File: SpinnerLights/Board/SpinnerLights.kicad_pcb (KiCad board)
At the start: 2 copper layers, 0 parts

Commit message: SpinnerLights: Initial board generation
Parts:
- added BT1: BAT-HLD-001-THM, BAT_BAT-HLD-001-THM, F.Cu at (197.2, 74.2)
- added BT2: BAT-HLD-001-THM, BAT_BAT-HLD-001-THM, F.Cu at (197.2, 54.9)
- added C1: 0.1uF, Capacitor_SMD:C_0805_2012Metric, F.Cu at (196.6, 85.4)
- added D1: D, Diode_SMD:D_0603_1608Metric_Pad1.05x0.95mm_HandSolder, F.Cu at (239.4, 51.6)
- added JP1: Jumper_2_Open, Jumper:SolderJumper-2_P1.3mm_Open_RoundedPad1.0x1.5mm, F.Cu at (239.3, 54.6)
- added JP2: Jumper_2_Open, Jumper:SolderJumper-2_P1.3mm_Open_RoundedPad1.0x1.5mm, F.Cu at (218.8, 75.8)
- added PIXEL2: NeoPixel_THT, LED_SMD:LED_SK6812MINI_PLCC4_3.5x3.5mm_P1.75mm, F.Cu at (213.1, 76.5)
- added PIXEL3: NeoPixel_THT, LED_SMD:LED_SK6812MINI_PLCC4_3.5x3.5mm_P1.75mm, F.Cu at (240.7, 47.7)
- added PIXEL4: NeoPixel_THT, LED_SMD:LED_SK6812MINI_PLCC4_3.5x3.5mm_P1.75mm, F.Cu at (213.1, 71.5)
- added PIXEL5: NeoPixel_THT, LED_SMD:LED_SK6812MINI_PLCC4_3.5x3.5mm_P1.75mm, F.Cu at (233.6, 52.8)
- added PIXEL6: NeoPixel_THT, LED_SMD:LED_SK6812MINI_PLCC4_3.5x3.5mm_P1.75mm, F.Cu at (220.1, 71.5)
- added Pixel1: NeoPixel_THT, LED_SMD:LED_SK6812MINI_PLCC4_3.5x3.5mm_P1.75mm, F.Cu at (233.6, 47.7)
- added R1: 10K, Resistor_SMD:R_0805_2012Metric_Pad1.20x1.40mm_HandSolder, F.Cu at (187.3, 85.4)
- added R2: 5K, Resistor_SMD:R_0805_2012Metric_Pad1.20x1.40mm_HandSolder, F.Cu at (192.0, 85.4)
- added R3: 400, Resistor_SMD:R_0805_2012Metric_Pad1.20x1.40mm_HandSolder, F.Cu at (211.9, 80.5)
- added U1: SeeeduinoXIAO, Seeeduino_XIAO:Seeeduino XIAO-MOUDLE14P-2.54-21X17.8MM, F.Cu at (211.3, 68.2)
- added U2: ADXL343, Package_LGA:LGA-14_3x5mm_P0.8mm_LayoutBorder1x6y, F.Cu at (232.4, 58.6)

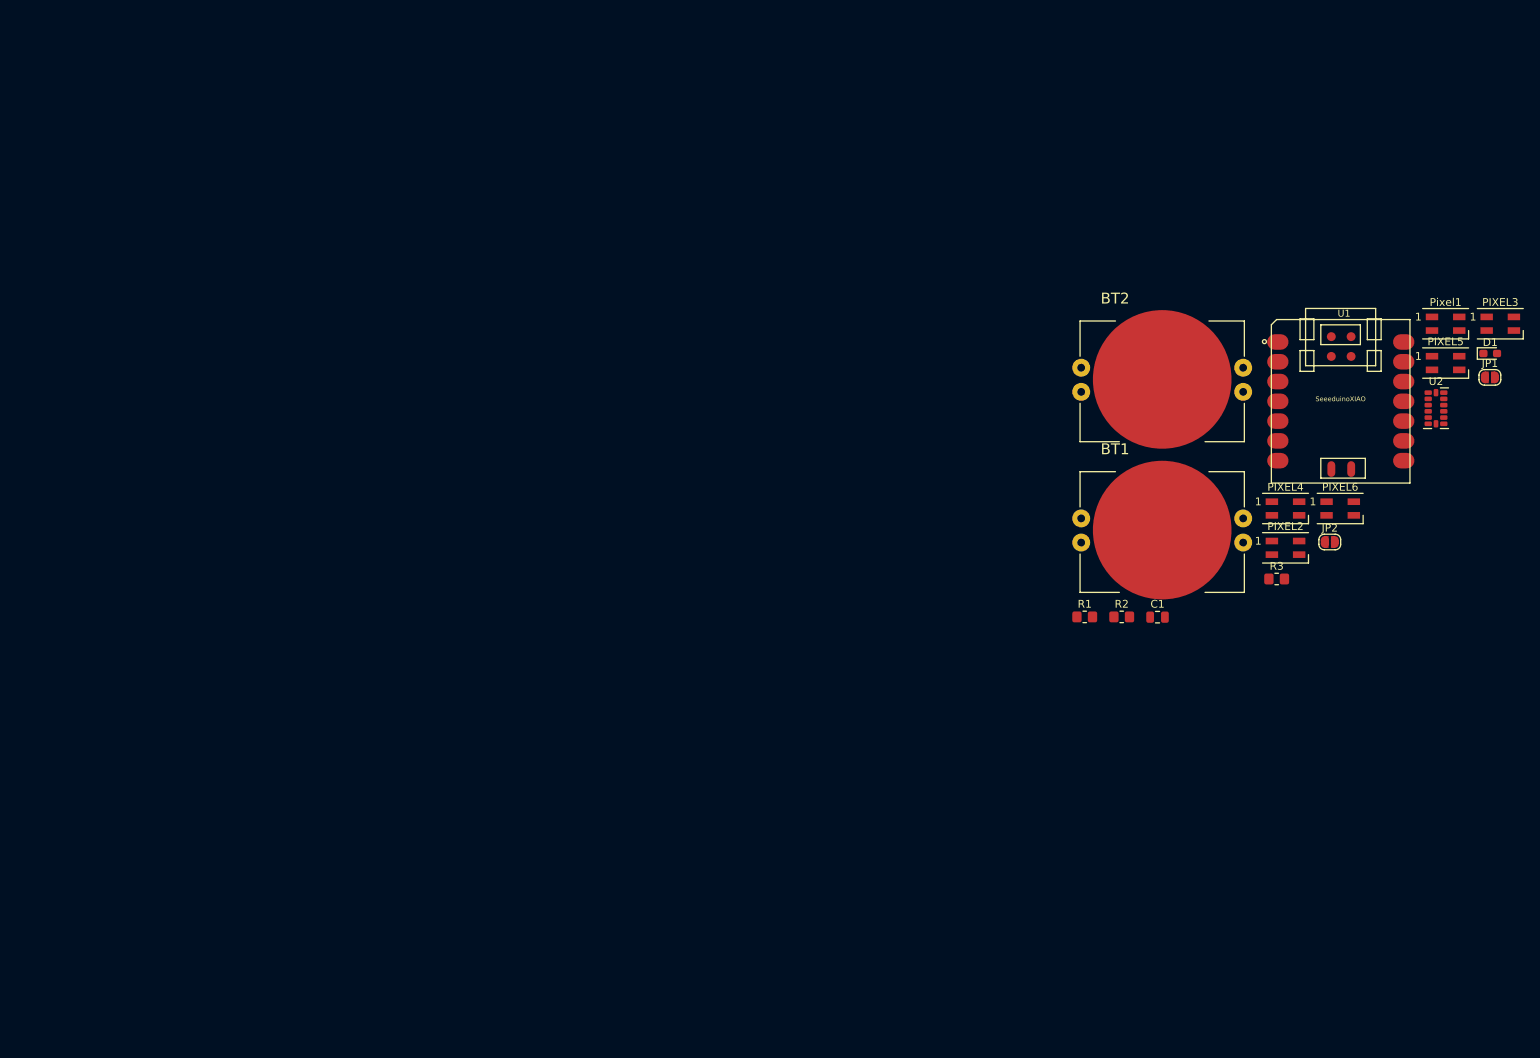
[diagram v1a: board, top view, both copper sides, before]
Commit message: SpinnerLights: More progress on board layout
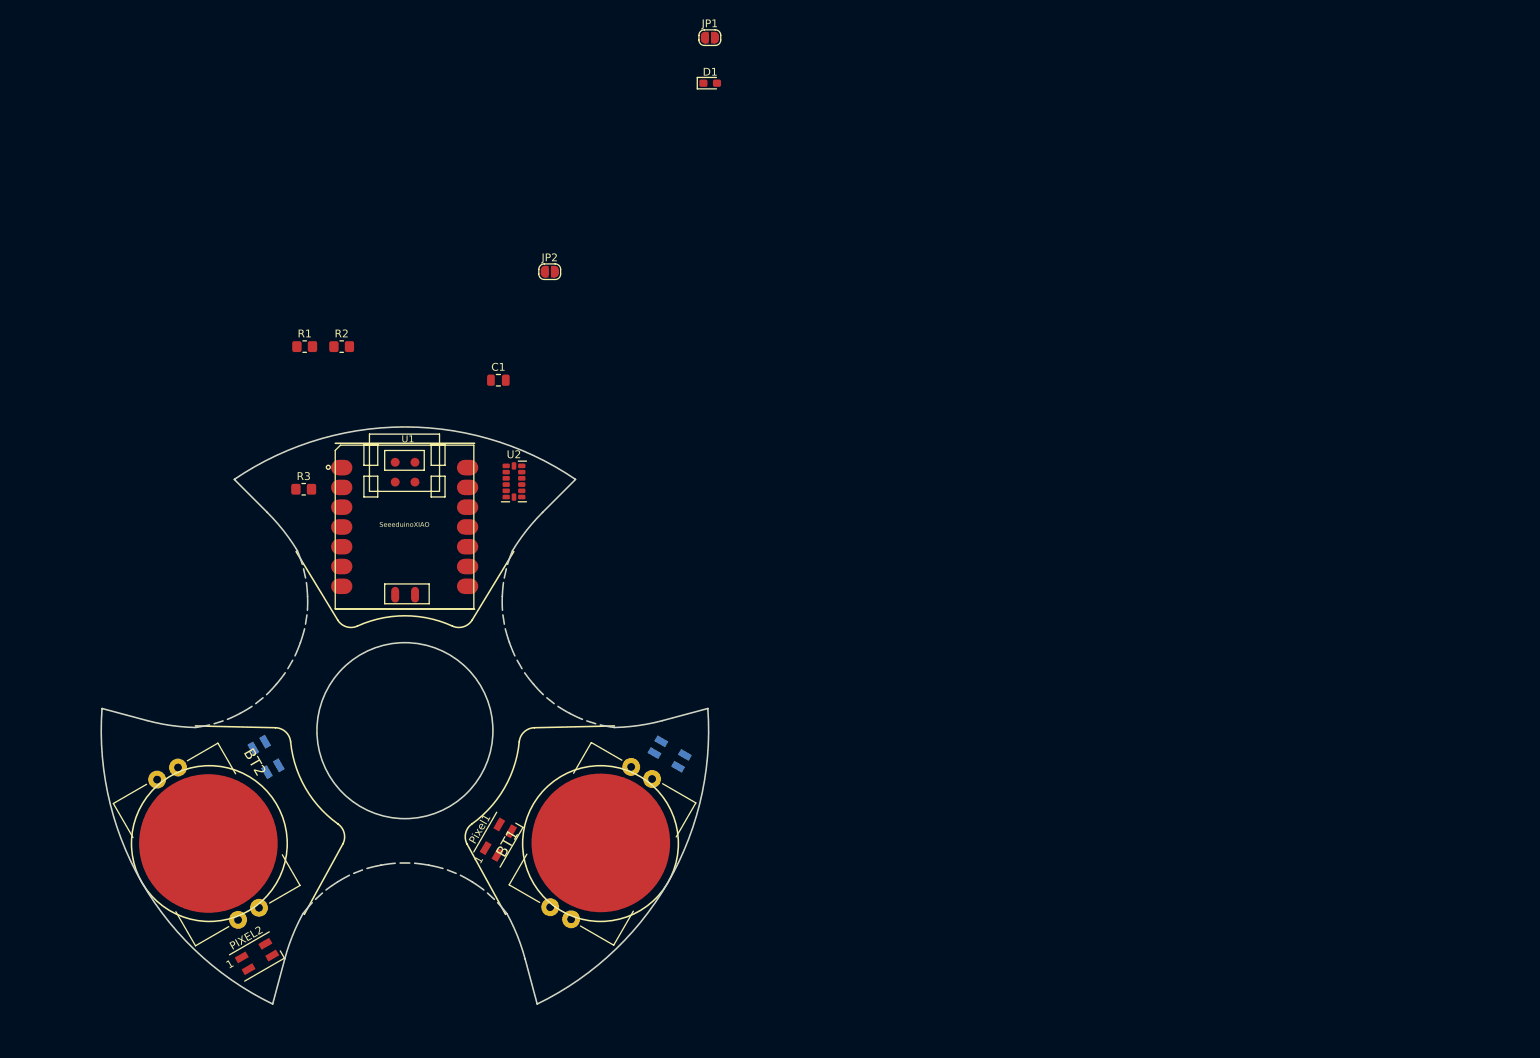
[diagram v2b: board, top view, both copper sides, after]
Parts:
- removed PIXEL5, PIXEL6: NeoPixel_THT, LED_SMD:LED_SK6812MINI_PLCC4_3.5x3.5mm_P1.75mm
- PIXEL3, PIXEL4: moved to B.Cu
- moved PIXEL3 168.0 mm to (82.2, 103.4), turned to 120 degrees
- moved PIXEL2 142.1 mm to (81.0, 129.0), turned to 30 degrees
- moved Pixel1 138.5 mm to (112.0, 114.0), turned to 60 degrees
- moved BT2 136.2 mm to (74.8, 114.5), turned to 300 degrees
- moved R3 125.5 mm to (87.0, 69.0)
- moved U1 121.3 mm to (91.0, 84.3)
- moved U2 118.8 mm to (114.0, 68.0)
- moved JP1 109.3 mm to (139.2, 11.0)
- moved R1 106.0 mm to (87.1, 50.7)
- moved R2 106.0 mm to (91.9, 50.7)
- moved D1 106.0 mm to (139.2, 16.9)
- moved JP2 106.0 mm to (118.6, 41.1)
- moved C1 89.9 mm to (112.0, 55.0)
- moved PIXEL4 85.1 mm to (134.0, 103.0), turned to 330 degrees
- moved BT1 82.5 mm to (125.2, 114.4), turned to 60 degrees
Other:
- board outline added: 78 x 74.1 mm

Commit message: SpinnerLights: started laying down wires
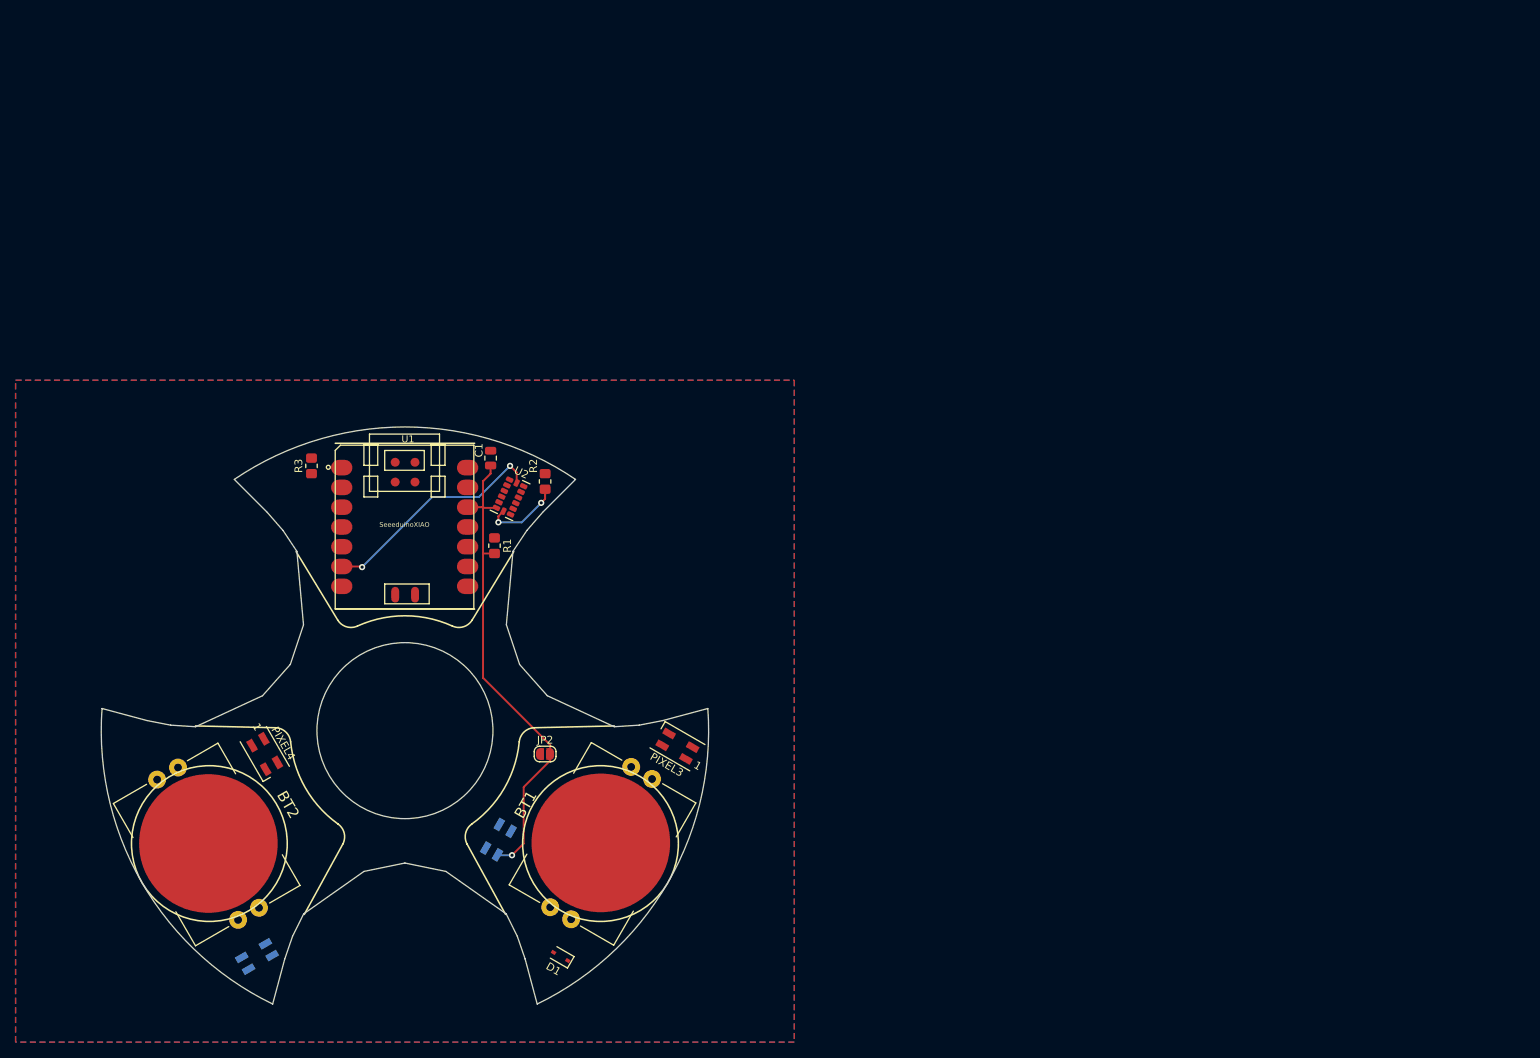
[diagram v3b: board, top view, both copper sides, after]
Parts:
- removed JP1: Jumper_2_Open, Jumper:SolderJumper-2_P1.3mm_Open_RoundedPad1.0x1.5mm
- BT1, BT2: footprint BAT_BAT-HLD-001-THM -> BAT-HLD-001-THM:BAT_BAT-HLD-001-THM
- D1: footprint Diode_SMD:D_0603_1608Metric_Pad1.05x0.95mm_HandSolder -> Diode_SMD:D_SOD-323
- PIXEL2, Pixel1: moved to B.Cu
- PIXEL3, PIXEL4: moved to F.Cu
- R2: value 5K -> 10K
- moved D1 113.8 mm to (120.0, 129.0), turned to 150 degrees
- moved JP2 61.9 mm to (118.0, 103.0)
- moved PIXEL3 52.9 mm to (135.0, 102.0), turned to 150 degrees
- moved PIXEL4 52.0 mm to (82.0, 103.0), turned to 300 degrees
- moved R1 35.3 mm to (111.5, 76.2), turned to 270 degrees
- moved R2 31.3 mm to (118.0, 68.0), turned to 90 degrees
- moved C1 10.0 mm to (111.0, 65.0), turned to 90 degrees
- moved R3 3.16 mm to (88.0, 66.0), turned to 90 degrees
- moved U2 2.06 mm to (113.5, 70.0), turned to 335 degrees
- turned PIXEL2 to 210 degrees
- turned Pixel1 to 240 degrees
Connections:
- BT2 pad N: Net-(BT2-PadN) -> GND
- D1 pad 2: Net-(D1-Pad2) -> Net-(BT1-PadP1)
- PIXEL3 pad 3: +3V3 -> Net-(JP2-Pad1)
- PIXEL4 pad 4: Net-(PIXEL4-Pad4) -> Net-(PIXEL3-Pad1)
- R1 pad 1: Net-(D1-Pad2) -> Net-(R1-Pad1)
- R2 pad 1: Net-(JP1-Pad2) -> Net-(R2-Pad1)
- U1 pad 14: Net-(U1-Pad14) -> Net-(D1-Pad1)
- U1 pad 15: Net-(BT1-PadP1) -> Net-(U1-Pad15)
- U1 pad 16: Net-(BT2-PadN) -> Net-(U1-Pad16)
- U1 pad 20: GND -> Net-(U1-Pad20)
- U2 pad 12: Net-(D1-Pad2) -> Net-(R1-Pad1)
- U2 pad 7: Net-(D1-Pad2) -> Net-(R2-Pad1)
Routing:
- net +3V3: track 0.00 -> 63.2 mm, vias 0 -> 1
- net SCL: track 0.00 -> 29.6 mm, vias 0 -> 2
- net Net-(R2-Pad1): track 0.00 -> 11.0 mm, vias 0 -> 2
- added copper zone on B.Cu, net GND
- added copper zone on F.Cu, net GND
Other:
- outline, holes or cut-outs redrawn

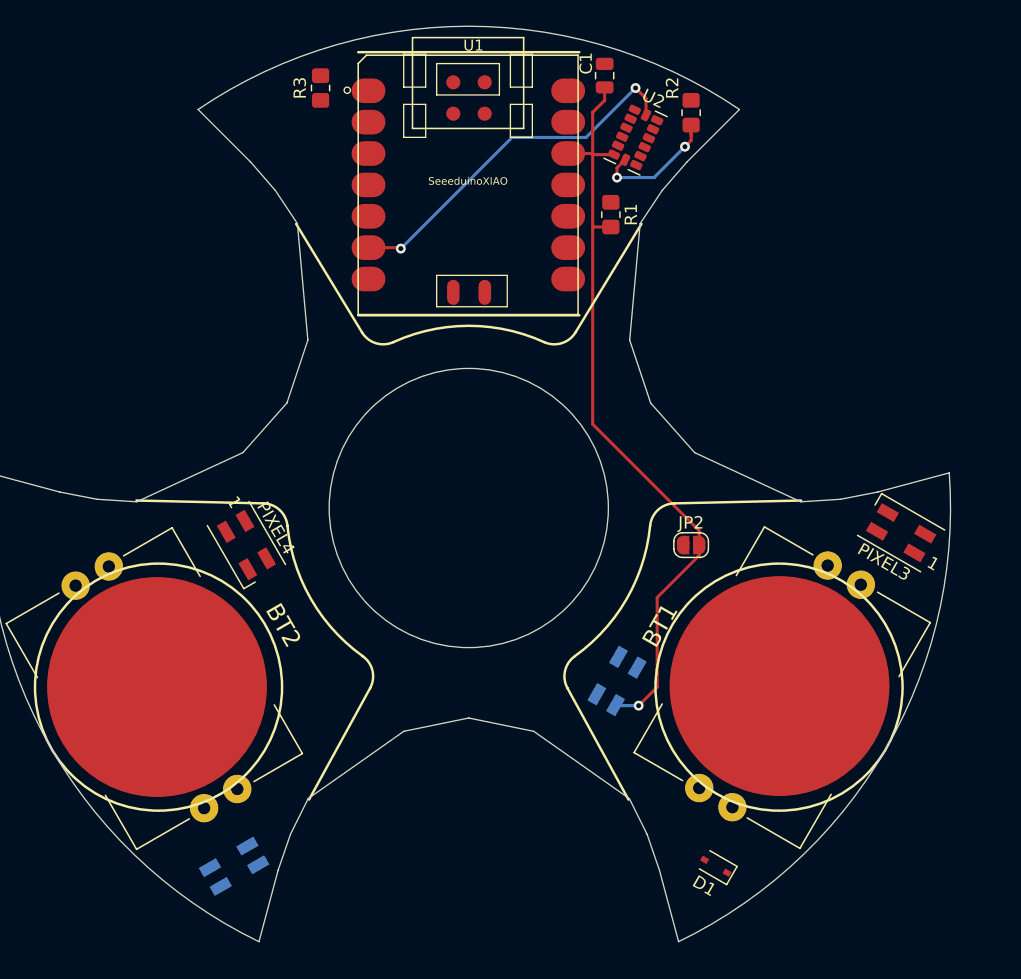
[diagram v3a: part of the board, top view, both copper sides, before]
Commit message: SpinnerLights: Almost complete routing
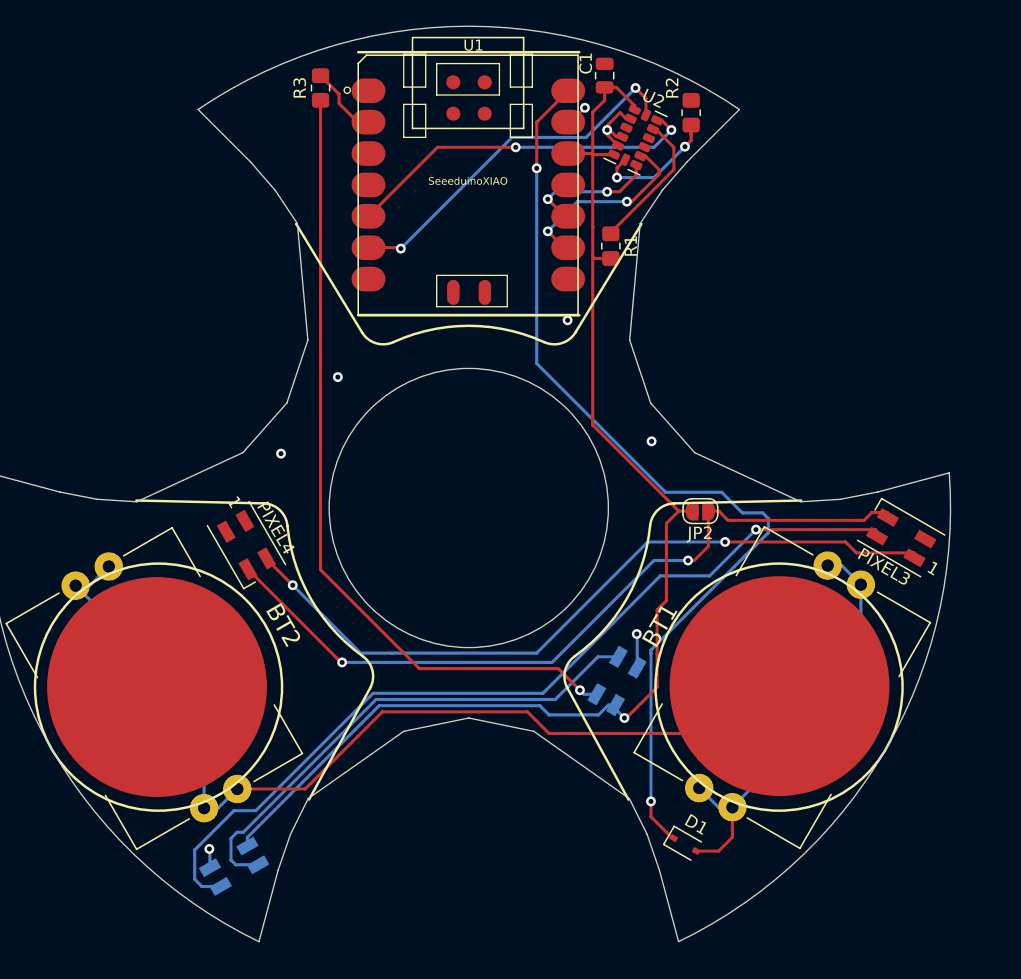
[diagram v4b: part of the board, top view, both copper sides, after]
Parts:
- moved D1 3.05 mm to (117.5, 127.2), turned to 330 degrees
- moved JP2 2.85 mm to (118.8, 100.2), turned to 180 degrees
- moved R1 2.55 mm to (111.5, 78.8)
- moved PIXEL3 0.40 mm to (135.0, 102.4)
- turned PIXEL2 to 30 degrees
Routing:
- net Net-(D1-Pad1): track 0.00 -> 77.9 mm, vias 0 -> 2
- net Net-(BT1-PadN): track 0.00 -> 77.8 mm
- net Net-(PIXEL2-Pad1): track 0.00 -> 70.8 mm, vias 0 -> 1
- net Net-(Pixel1-Pad4): track 0.00 -> 64.5 mm, vias 0 -> 1
- net Net-(JP2-Pad1): track 0.00 -> 62.2 mm, vias 0 -> 2
- net Net-(PIXEL3-Pad1): track 0.00 -> 59.7 mm, vias 0 -> 2
- net Net-(PIXEL2-Pad4): track 0.00 -> 41.6 mm
- net +3V3: track 63.2 -> 103.0 mm
- net Net-(BT1-PadP1): track 0.00 -> 34.8 mm
- net SDA: track 0.00 -> 28.9 mm, vias 0 -> 2
- net INT2: track 0.00 -> 15.5 mm, vias 0 -> 2
- net GND: track 0.00 -> 13.3 mm, vias 0 -> 8
- net Net-(R1-Pad1): track 0.00 -> 11.4 mm
- net INT1: track 0.00 -> 11.0 mm, vias 0 -> 2
- net Net-(R3-Pad2): track 0.00 -> 5.88 mm
